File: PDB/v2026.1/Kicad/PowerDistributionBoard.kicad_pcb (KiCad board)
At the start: 2 copper layers, 97.2 x 112.4 mm, 66 parts, among them J1 12V_EXP3, J10 BMS, J11 IMD, J12 Suspension_Linear_Pot1, J13 Suspension_Linear_Pot2, J14 Suspension_Linear_Pot3, J15 Suspension_Lin_Pot4, J16 CCM_Faults, J17 EXP1_5V, J18 RasPI_5V, J19 LATCH_12V, J2 12V_EXP2, J20 Throttle_Sensor, J21 Current_Sensor, J24 Wheel_Sensor1, J25 Wheel_Sensor2, J26 3V3_EXP, J27 BATTERY_12V, J28 BATTERY_GND, J29 BATTERY_24V, J3 12V_EXP1, J31 FAN1_24V, J32 FAN2_24V, J33 PUMP1_24V, J34 PUMP2_24V, J35 24V_EXP1, J4 RTM, J5 CCM_12V, J7 BSPD, J8 LATCH, J9 TSSI, U1 5to3.3_Linear_Regulator, U2 TLV76150DCYR

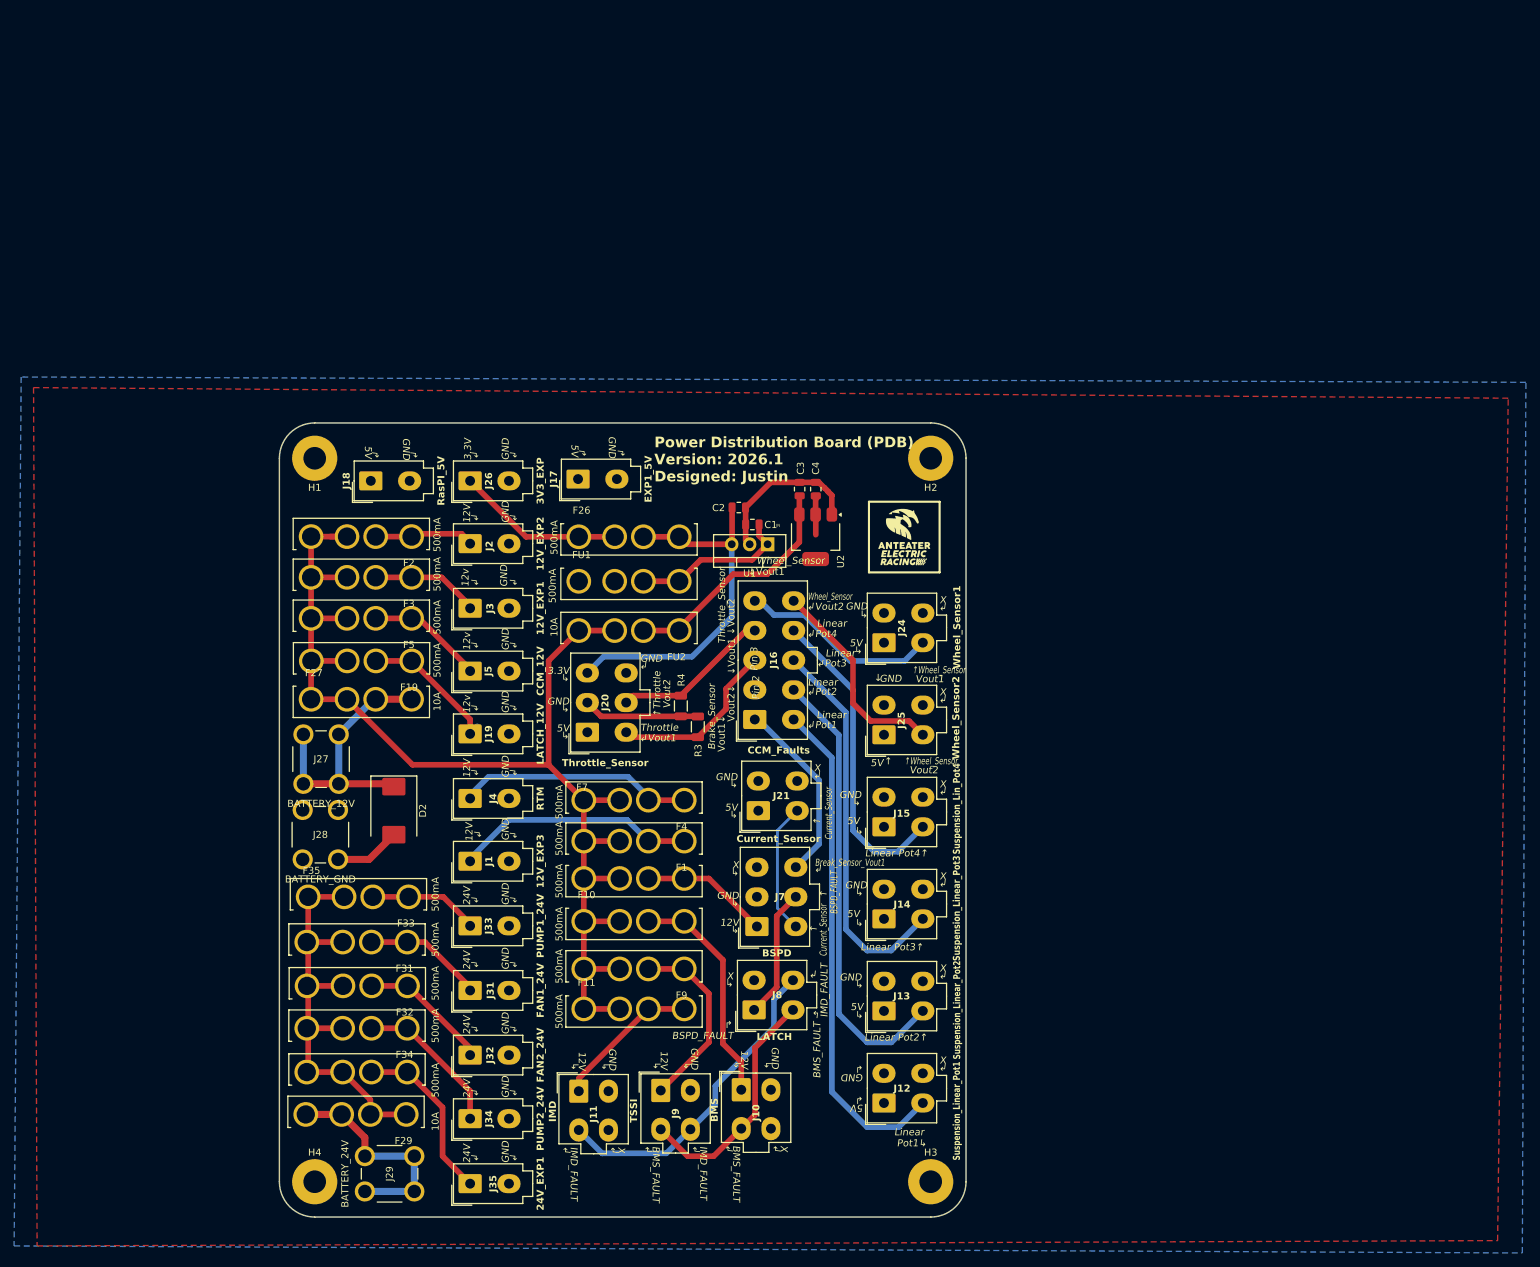
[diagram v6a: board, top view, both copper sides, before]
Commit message: Reduced PDB size, power planes just started
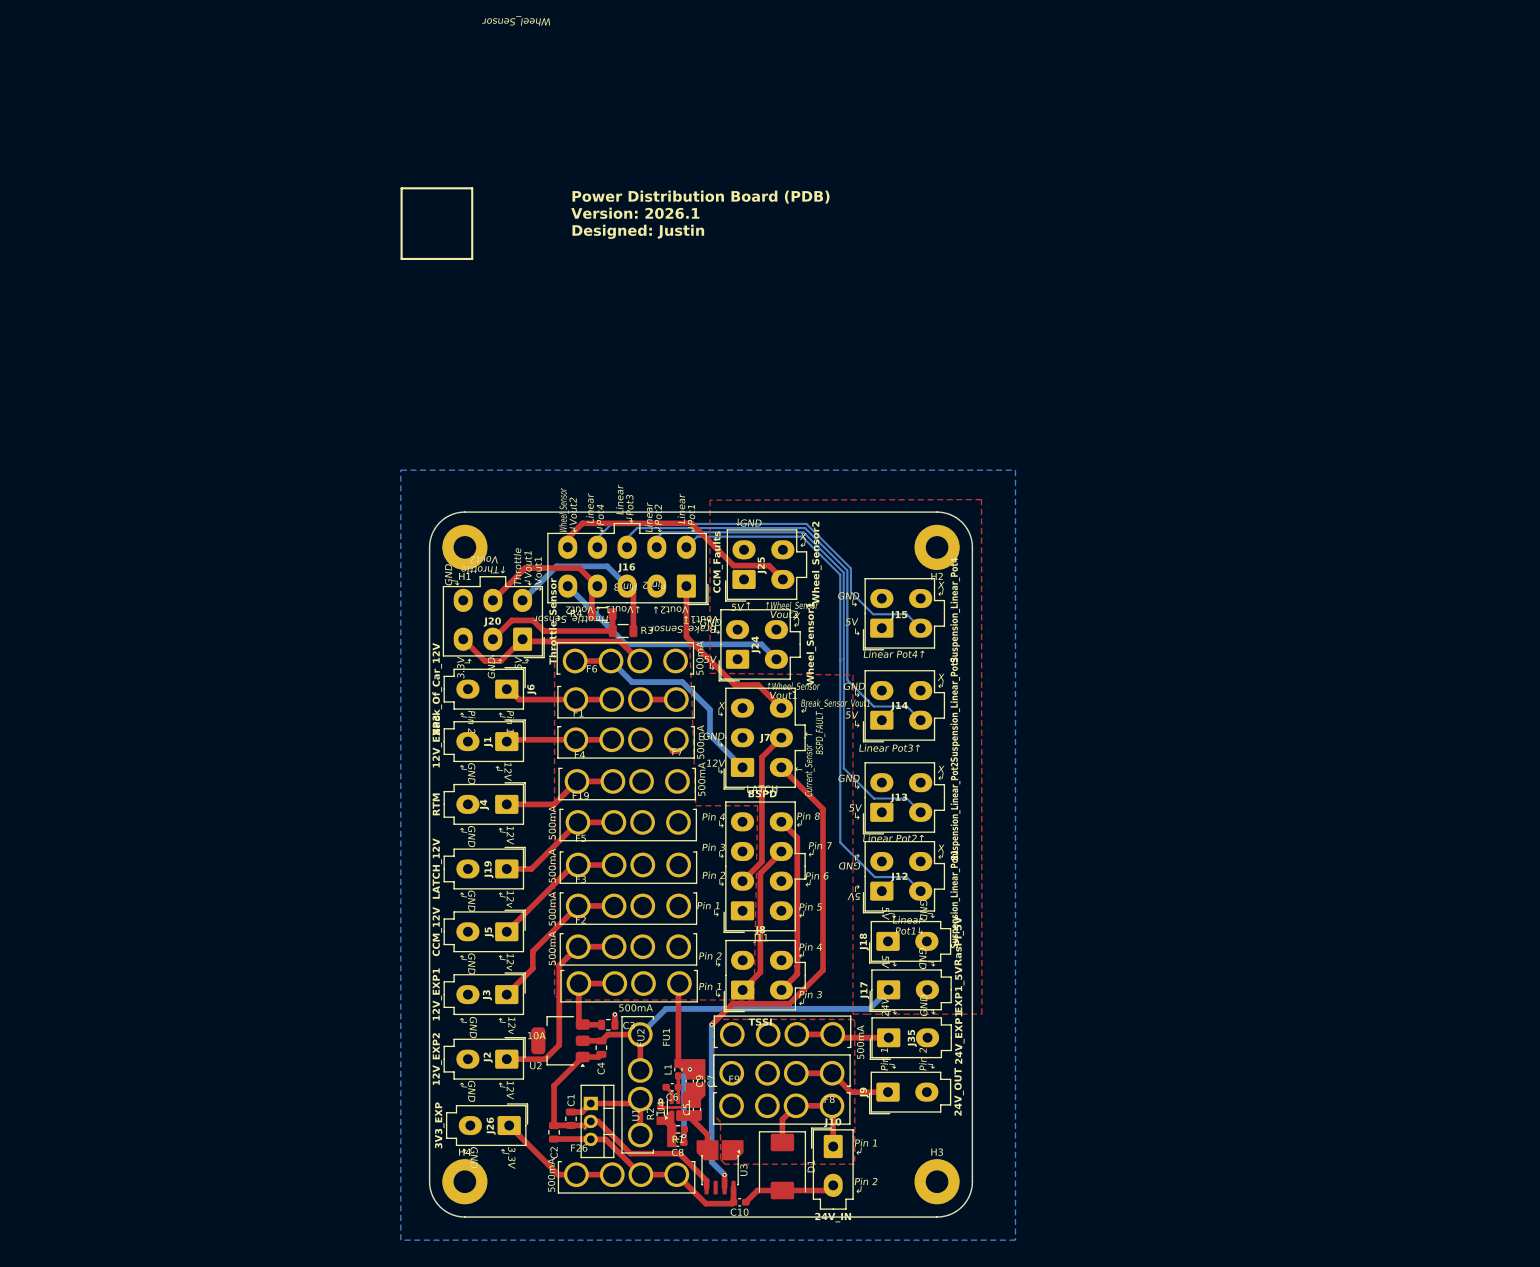
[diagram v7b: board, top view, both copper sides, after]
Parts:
- removed D2: 1.5SMCxxA, Diode_SMD:D_SMC
- removed F10, F11, F31, F32, F33, F34: 500mA, 0footprints:FUSE_3522-2
- removed F27, F29: 10A, 0footprints:FUSE_3522-2
- removed J21: Current_Sensor, 0footprints:Molex_Mini-Fit_Jr_5566-04A_2x02_P4.20mm_Vertical
- removed J27: BATTERY_12V, 0footprints:KEYSTONE_7797
- removed J28: BATTERY_GND, 0footprints:KEYSTONE_7797
- removed J29: BATTERY_24V, 0footprints:KEYSTONE_7797
- removed J31: FAN1_24V, 0footprints:Molex_Mini-Fit_Jr_5566-02A_2x01_P4.20mm_Vertical
- removed J32: FAN2_24V, 0footprints:Molex_Mini-Fit_Jr_5566-02A_2x01_P4.20mm_Vertical
- removed J33: PUMP1_24V, 0footprints:Molex_Mini-Fit_Jr_5566-02A_2x01_P4.20mm_Vertical
- removed J34: PUMP2_24V, 0footprints:Molex_Mini-Fit_Jr_5566-02A_2x01_P4.20mm_Vertical
- removed the REF** at (154.0, 40.8)
- added C10: 100nF, Capacitor_SMD:C_0603_1608Metric_Pad1.08x0.95mm_HandSolder, F.Cu at (131.0, 134.6)
- added C5: 10uF, Capacitor_SMD:C_0603_1608Metric_Pad1.08x0.95mm_HandSolder, F.Cu at (124.9, 121.5)
- added C6: 100nF, Capacitor_SMD:C_0603_1608Metric_Pad1.08x0.95mm_HandSolder, F.Cu at (121.4, 118.3)
- added C7: 22uF, Capacitor_SMD:C_0603_1608Metric_Pad1.08x0.95mm_HandSolder, F.Cu at (125.5, 117.5)
- added C8: 56pF, Capacitor_SMD:C_0603_1608Metric_Pad1.08x0.95mm_HandSolder, F.Cu at (122.2, 126.2)
- added C9: 22uF, Capacitor_SMD:C_0603_1608Metric_Pad1.08x0.95mm_HandSolder, F.Cu at (123.9, 117.5)
- added D1: 1.5SMCxxA, Diode_SMD:D_SMC, F.Cu at (137.0, 129.6)
- added F6: 500mA, 0footprints:FUSE_3522-2, F.Cu at (114.9, 63.8)
- added F8: 500mA, 0footprints:FUSE_3522-2, F.Cu at (136.9, 116.0)
- added J6: Back_Of_Car_12V, 0footprints:Molex_Mini-Fit_Jr_5566-02A_2x01_P4.20mm_Vertical, F.Cu at (98.0, 62.0)
- added L1: 10uH, Inductor_SMD:L_0603_1608Metric_Pad1.05x0.95mm_HandSolder, F.Cu at (122.3, 115.9)
- added R1: 249k, Resistor_SMD:R_0603_1608Metric_Pad0.98x0.95mm_HandSolder, F.Cu at (122.2, 124.3)
- added R2: 18k, Resistor_SMD:R_0603_1608Metric_Pad0.98x0.95mm_HandSolder, F.Cu at (119.8, 122.1)
- added U3: ACS711xLCTR-12AB, Package_SO:SOIC-8_3.9x4.9mm_P1.27mm, F.Cu at (128.2, 130.1)
- added U4: AP63200WU, Package_TO_SOT_SMD:TSOT-23-6, F.Cu at (122.3, 121.2)
- F9: value 500mA -> 10A
- J10: value BMS -> 24V_IN; footprint 0footprints:Molex_Mini-Fit_Jr_5566-04A_2x02_P4.20mm_Vertical -> 0footprints:Molex_Mini-Fit_Jr_5566-02A_2x01_P4.20mm_Vertical
- J11: value IMD -> LATCH; footprint 0footprints:Molex_Mini-Fit_Jr_5566-04A_2x02_P4.20mm_Vertical -> 0footprints:Molex_Mini-Fit_Jr_5566-08A_2x04_P4.20mm_Vertical
- J15: value Suspension_Lin_Pot4 -> Suspension_Linear_Pot4
- J8: value LATCH -> TSSI
- J9: value TSSI -> 24V_OUT; footprint 0footprints:Molex_Mini-Fit_Jr_5566-04A_2x02_P4.20mm_Vertical -> 0footprints:Molex_Mini-Fit_Jr_5566-02A_2x01_P4.20mm_Vertical
- moved J18 98.0 mm to (152.0, 97.7)
- moved C2 92.2 mm to (104.7, 124.7), turned to 90 degrees
- moved J26 91.4 mm to (98.3, 123.8), turned to -90 degrees
- moved F26 90.3 mm to (115.0, 131.1)
- moved C1 88.0 mm to (107.1, 122.8), turned to -90 degrees
- moved C4 84.7 mm to (111.4, 112.7), turned to -90 degrees
- moved J17 84.6 mm to (152.0, 104.6)
- moved U1 83.0 mm to (109.9, 120.7), turned to -90 degrees
- moved C3 80.5 mm to (112.4, 109.5), turned to 0 degrees
- moved U2 80.0 mm to (105.6, 111.8), turned to 180 degrees
- moved J2 73.2 mm to (98.0, 114.4), turned to -90 degrees
- moved FU1 70.9 mm to (116.5, 118.0), turned to -90 degrees
- moved F2 69.9 mm to (115.2, 98.8), turned to 0 degrees
- moved J35 62.8 mm to (152.1, 111.3)
- moved F3 60.5 mm to (115.2, 93.1), turned to 0 degrees
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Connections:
- F9 pad 1: /Fuse_TSSI -> 24V
- F9 pad 2: 12V -> Net-(D1-A1)
- J10 pad 1: /Fuse_BMMS -> Net-(D1-A1)
- J11 pad 1: /Fuse_IMD -> unconnected-(J11-Pin_1-Pad1)
- J11 pad 2: GND -> BSPD_FAULT
- J11 pad 3: IMD_FAULT -> 12V
- J11 pad 4: unconnected-(J11-Pin_4-Pad4) -> GND
- J20 pad 1: 5V -> 12V
- J20 pad 3: 3.3V -> 12V
- J8 pad 1: BSPD_FAULT -> GLV
- J8 pad 2: unconnected-(J8-Pin_2-Pad2) -> GND
- J8 pad 3: BMS_FAULT -> bms_imd_latch_only
- J8 pad 4: IMD_FAULT -> unconnected-(J8-Pin_4-Pad4)
- J9 pad 1: /Fuse_TSSI -> /Fuse_24V_OUT
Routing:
- net 12V: track 177.3 -> 58.2 mm, vias 0 -> 2
- net 24V: track 63.0 -> 0.00 mm
- net Current_Sensor: track 19.5 -> 73.9 mm, vias 0 -> 2
- net 5V: track 5.53 -> 51.4 mm
- net IMD_FAULT: track 45.7 -> 0.00 mm
- net /Fuse_Batt12V: track 39.3 -> 0.00 mm
- net BMS_FAULT: track 34.4 -> 0.00 mm
- net GND: track 49.4 -> 83.7 mm, vias 0 -> 2
- net /Fuse_BMMS: track 32.7 -> 0.00 mm
- net /Fuse_Batt24V: track 31.3 -> 0.00 mm
- net /Fuse_TSSI: track 25.9 -> 0.00 mm
- net bms_imd_latch_only: track 0.00 -> 25.7 mm
- net GLV: track 0.00 -> 21.9 mm
- net /Fuse_Pump2: track 21.6 -> 0.00 mm
- net /Fuse_IMD: track 20.9 -> 0.00 mm
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- added copper zone on F.Cu, net 12V
- added copper zone on F.Cu, net 24V
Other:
- board size 97.2 x 112.4 mm -> 76.8 x 99.8 mm
- board text added: "${REFERENCE}"

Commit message: Finalized PDB silkscreen
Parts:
- added REF**: logo, 0footprints:logo, F.Cu at (144.8, 99.8)
- F1: value 500mA -> 12V_EXP3
- F19: value 500mA -> LATCH_12V
- F2: value 500mA -> 12V_EXP2
- F26: value 500mA -> 3V3_EXP
- F3: value 500mA -> 12V_EXP1
- F35: value 500mA -> 24V_EXP1
- F4: value 500mA -> RTM
- F5: value 500mA -> CCM_12V
- F6: value 500mA -> Back_Car_12V
- F7: value 500mA -> BSPD
- F8: value 500mA -> 24V_OUT
- F9: value 10A -> 24V_IN
- FU1: value 500mA -> 3V3_LDO
- FU2: value 10A -> 5V_LDO
- J6: value Back_Of_Car_12V -> Back_Car_12V
- moved J12 37.4 mm to (149.2, 53.2)
- moved J15 36.6 mm to (149.2, 89.9)
- moved J13 14.4 mm to (149.2, 65.2)
- moved J14 11.2 mm to (149.2, 77.4)
- moved J9 3.22 mm to (152.6, 122.2)
- moved J35 1.89 mm to (152.4, 113.2)
- moved J25 1.63 mm to (133.2, 46.5)
- moved J7 0.72 mm to (131.4, 73.8)
- moved J1 0.58 mm to (98.0, 70.0)
- moved J17 0.57 mm to (152.4, 105.0)
- moved J18 0.54 mm to (152.2, 97.2)
- renumbered H4 to M3, H2 to M3, H1 to M3, H3 to M3
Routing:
- net Linear_Pot4: track 56.0 -> 96.6 mm
- net Linear_Pot1: track 76.8 -> 38.5 mm
- net 12V: track 58.2 -> 24.3 mm
- net 3.3V: track 31.4 -> 7.30 mm
- net Linear_Pot3: track 63.8 -> 78.7 mm
- net Linear_Pot2: track 71.6 -> 60.8 mm
- net /Fuse_EXP2_12V: track 28.4 -> 25.2 mm
- net Current_Sensor: track 73.9 -> 71.0 mm
- net /Fuse_24V_OUT: track 14.1 -> 16.0 mm
- net Wheel_Sensor_Vout2: track 35.9 -> 34.0 mm
- net Throttle_Sensor_Vout1: track 24.7 -> 26.6 mm
- net /Fuse_BSPD: track 32.0 -> 33.4 mm
- net /Fuse_EXP1_24V: track 13.2 -> 14.3 mm
- net /Fuse_EXP3_12V: track 15.0 -> 15.9 mm
- net BSPD_FAULT: track 22.6 -> 21.9 mm
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- added copper zone on F.Cu, net 3.3V
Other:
- board text added: "24V"
- board text added: "Break"
- board text added: "Possible Improvements: - Decoupling Capacitors across power plane splits - Run Ansys sim. to double check - Add filters to ensure clean signal for Current Sensor & more... - Follow this guide: https://www.allpcb.com/blog/pcb-knowledge/splitting-power-planes-when-and-why-to-divide-your-pcbs-power.html - ENSURE A CONTINOUS GND PLANE (less noisy) - Reroute and optimize placements again"
- board text added: "Throttle"
- board text added: "Vout1↓"
- board text added: "Wheel"
- board text added: "↲Pot2"
- board text added: "↲Pot3"
- board text added: "↲Pot4"
- board text added: "↳"
- board text removed: "${REFERENCE}"
